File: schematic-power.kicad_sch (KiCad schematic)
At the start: 20 parts, among them U9 TPS62933

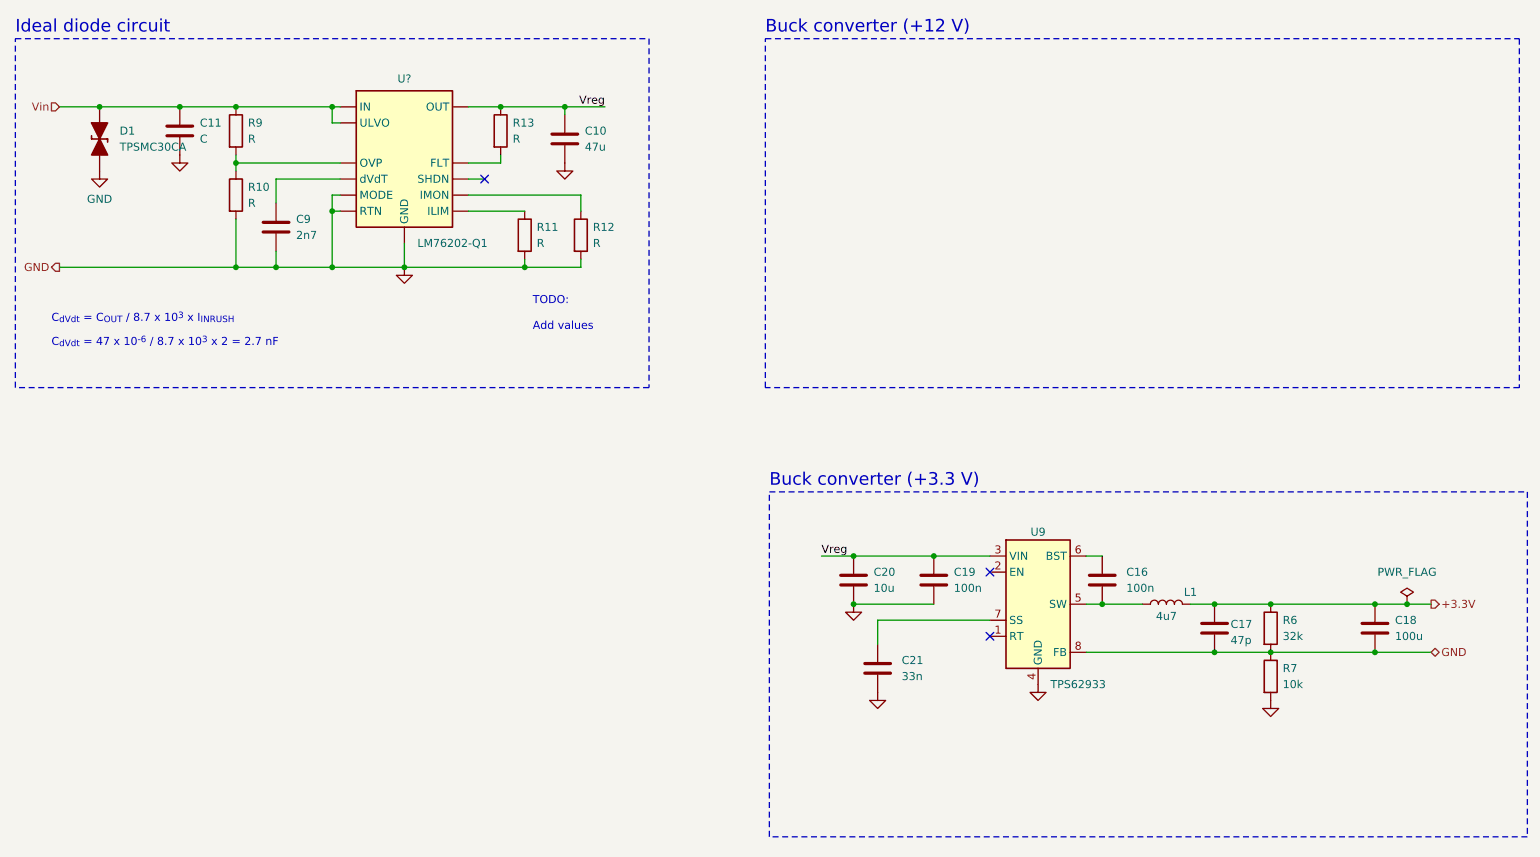
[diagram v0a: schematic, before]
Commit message: Add power stages
Valve, power supplay, fan
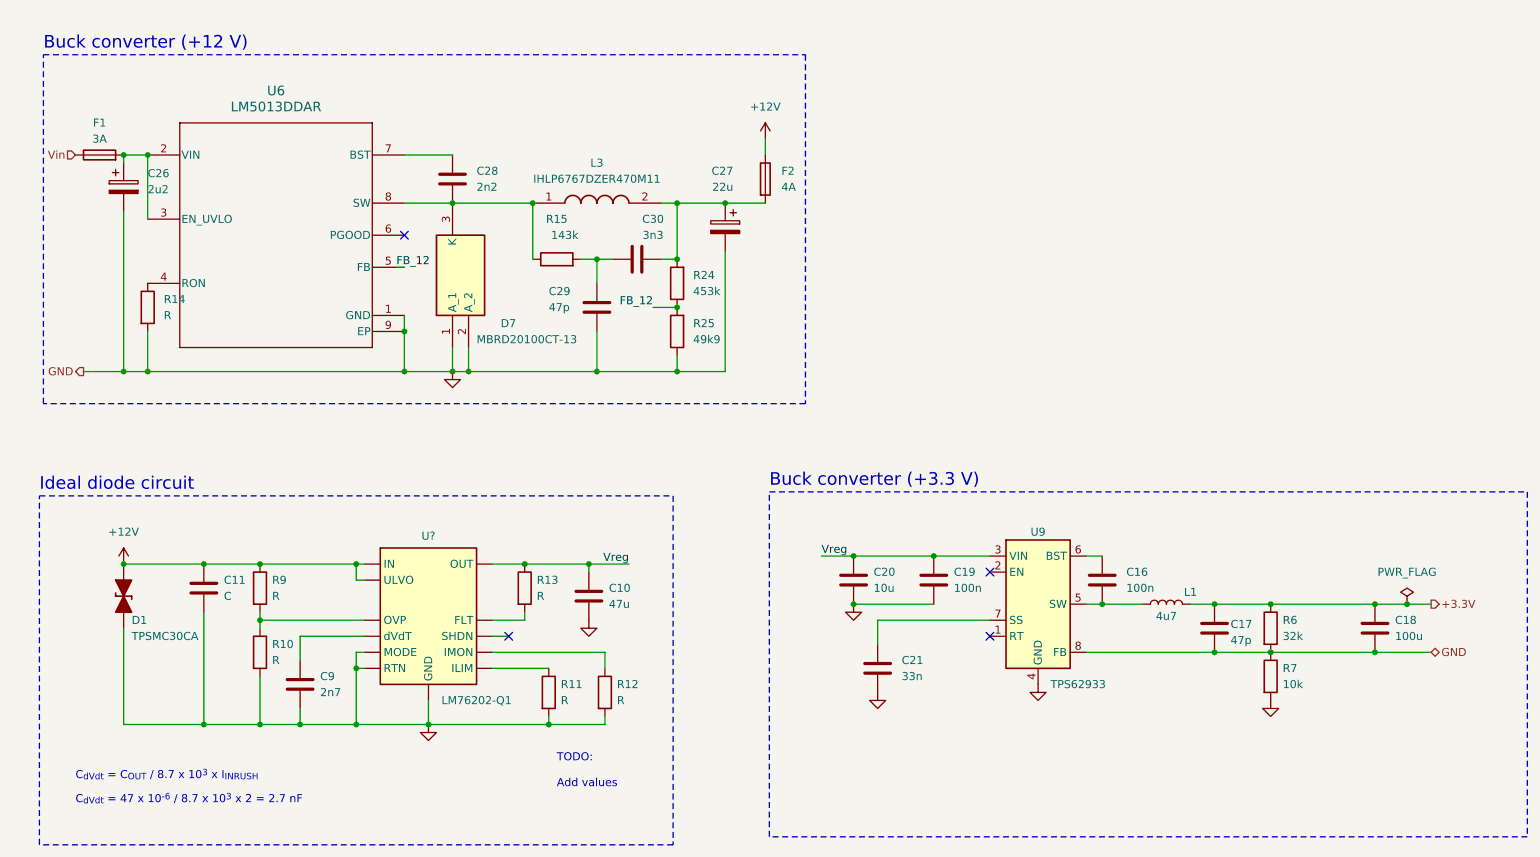
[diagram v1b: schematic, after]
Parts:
- added C26: 2u2, symbol Device:C_Polarized
- added C27: 22u, symbol Device:C_Polarized
- added C28: 2n2, symbol Device:C
- added C29: 47p, symbol Device:C
- added C30: 3n3, symbol Device:C
- added D7: MBRD20100CT-13, TO252_(DPAK)_1, symbol MBRD20100CT-13:MBRD20100CT-13
- added F1: 3A, symbol Device:Fuse
- added F2: 4A, symbol Device:Fuse
- added L3: IHLP6767DZER470M11, IHLP6767DZER470M11, symbol IHLP6767DZER470M11:IHLP6767DZER470M11
- added R14: R, symbol Device:R
- added R15: 143k, symbol Device:R
- added R24: 453k, symbol Device:R
- added R25: 49k9, symbol Device:R
- added U6: LM5013DDAR, DDA0008E-IPC_A, symbol 2023-11-20_17-31-45:LM5013DDAR
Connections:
- net GND: now also C26.2, C27.2, C29.1, D7.1 (A_1), D7.2 (A_2), R14.2, R25.1, U6.1 (GND), U6.9 (EP)
- net Vin: now also F1.1; no longer C11.1, D1.2 (A), R9.1, U?. (dVdT)
- new net: C28.1, D7.3 (K), L3.1, R15.1, U6.8 (SW)
- new net: C27.1, C30.2, F2.2, L3.2, R24.2
- new net: C26.1, F1.2, U6.2 (VIN), U6.3 (EN_UVLO)
- new net: C29.2, C30.1, R15.2
- new net: R14.1, U6.4 (RON)
- new net: C28.2, U6.7 (BST)
- new net +12V: C11.1, D1.2 (A), F2.1, R9.1, U?. (dVdT)
- new net FB_12: R24.1, R25.2, U6.5 (FB)
- no-connect marks 3 -> 4
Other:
- moved on the sheet: C10, C11, C9, D1, R10, R11, R12, R13, R9, U?

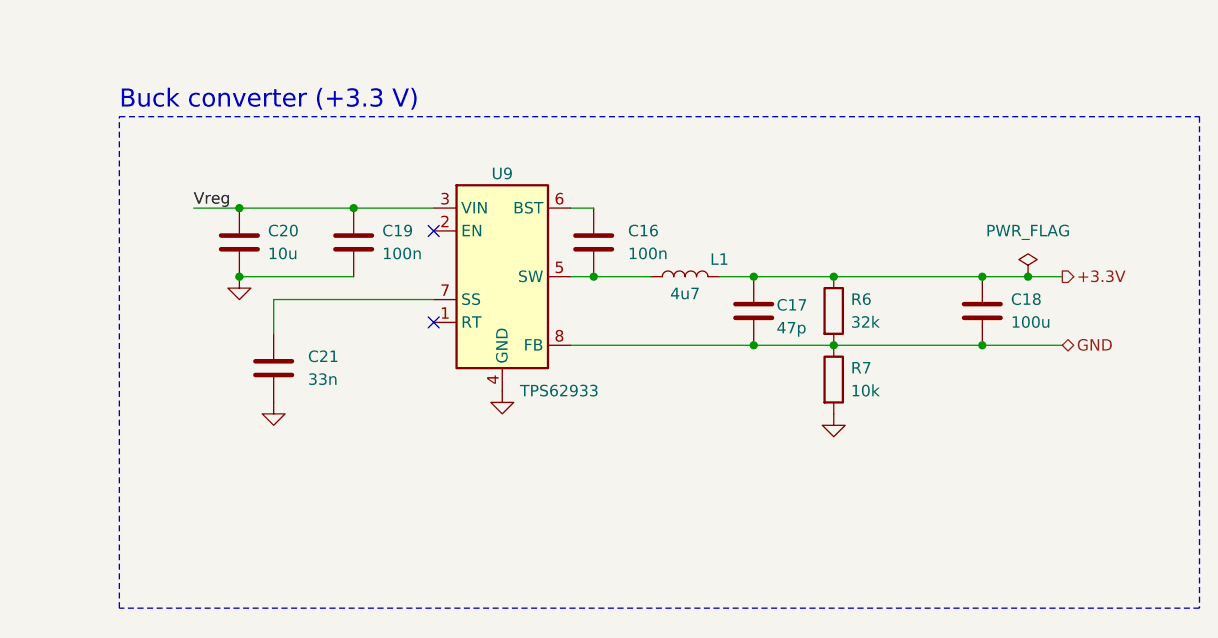
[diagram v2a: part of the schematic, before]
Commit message: Add Schottky Diode for VBUS and Vreg
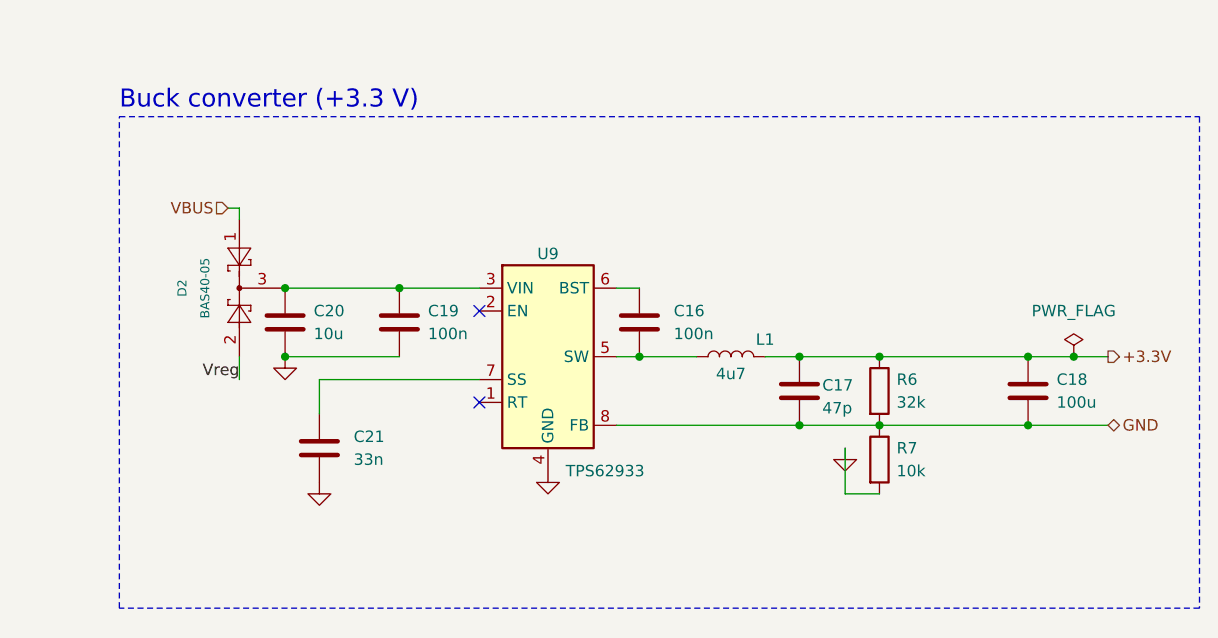
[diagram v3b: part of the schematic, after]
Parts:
- added D2: BAS40-05, Package_TO_SOT_SMD:SOT-23, symbol Diode:BAS40-04
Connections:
- net Vreg: now also D2.2; no longer C19.1, C20.1, U9.3 (VIN)
- new net: C19.1, C20.1, D2.3, U9.3 (VIN)
- new net VBUS: D2.1
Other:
- moved on the sheet: C16, C17, C18, C19, C20, C21, L1, R6, R7, U9

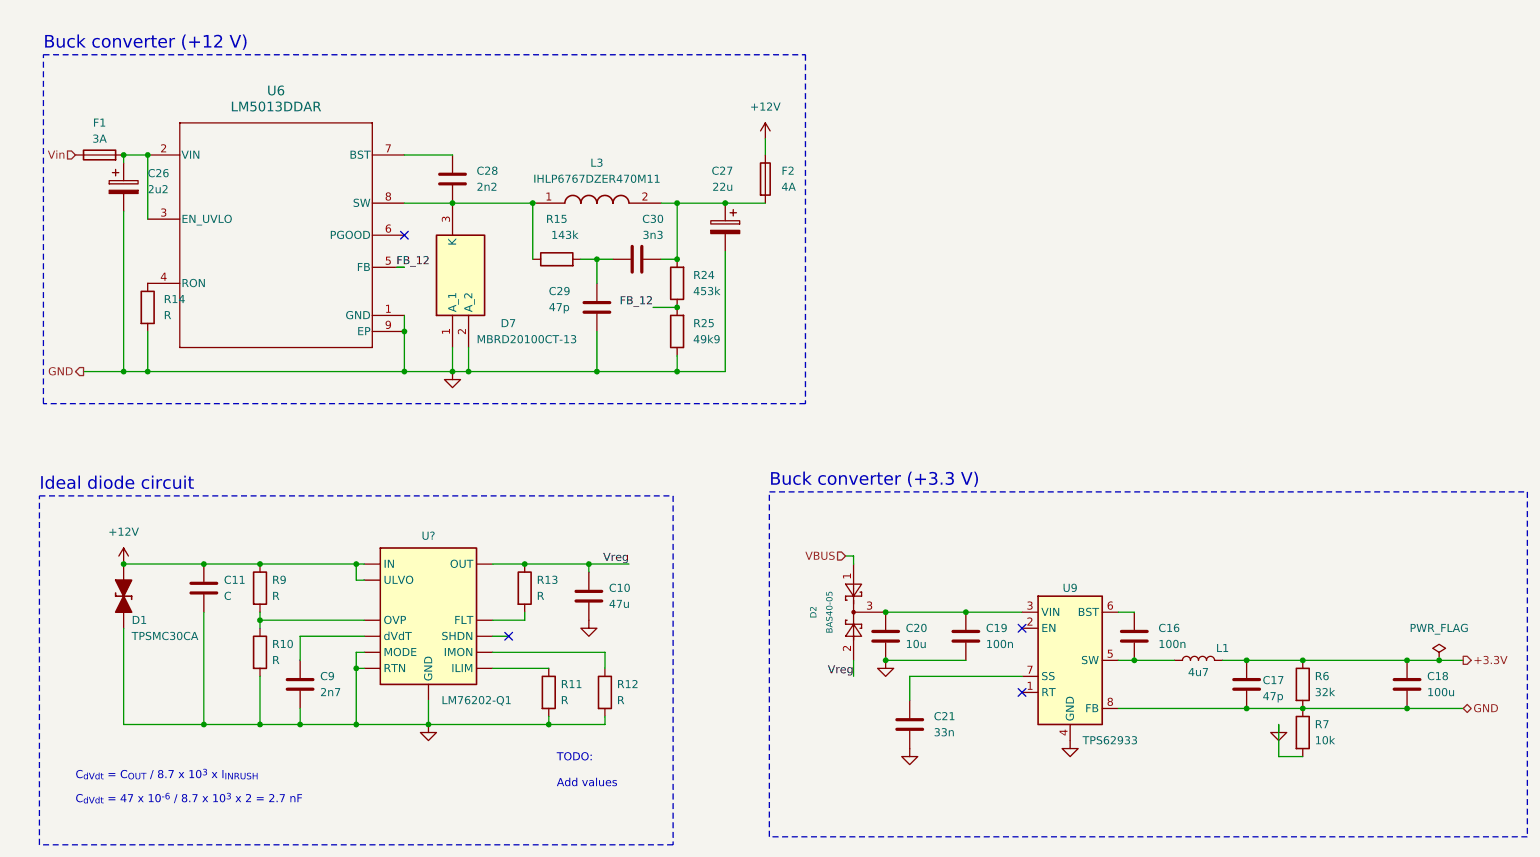
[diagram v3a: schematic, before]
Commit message: Add FC voltage measure, axilary input and output
Schematic complet?
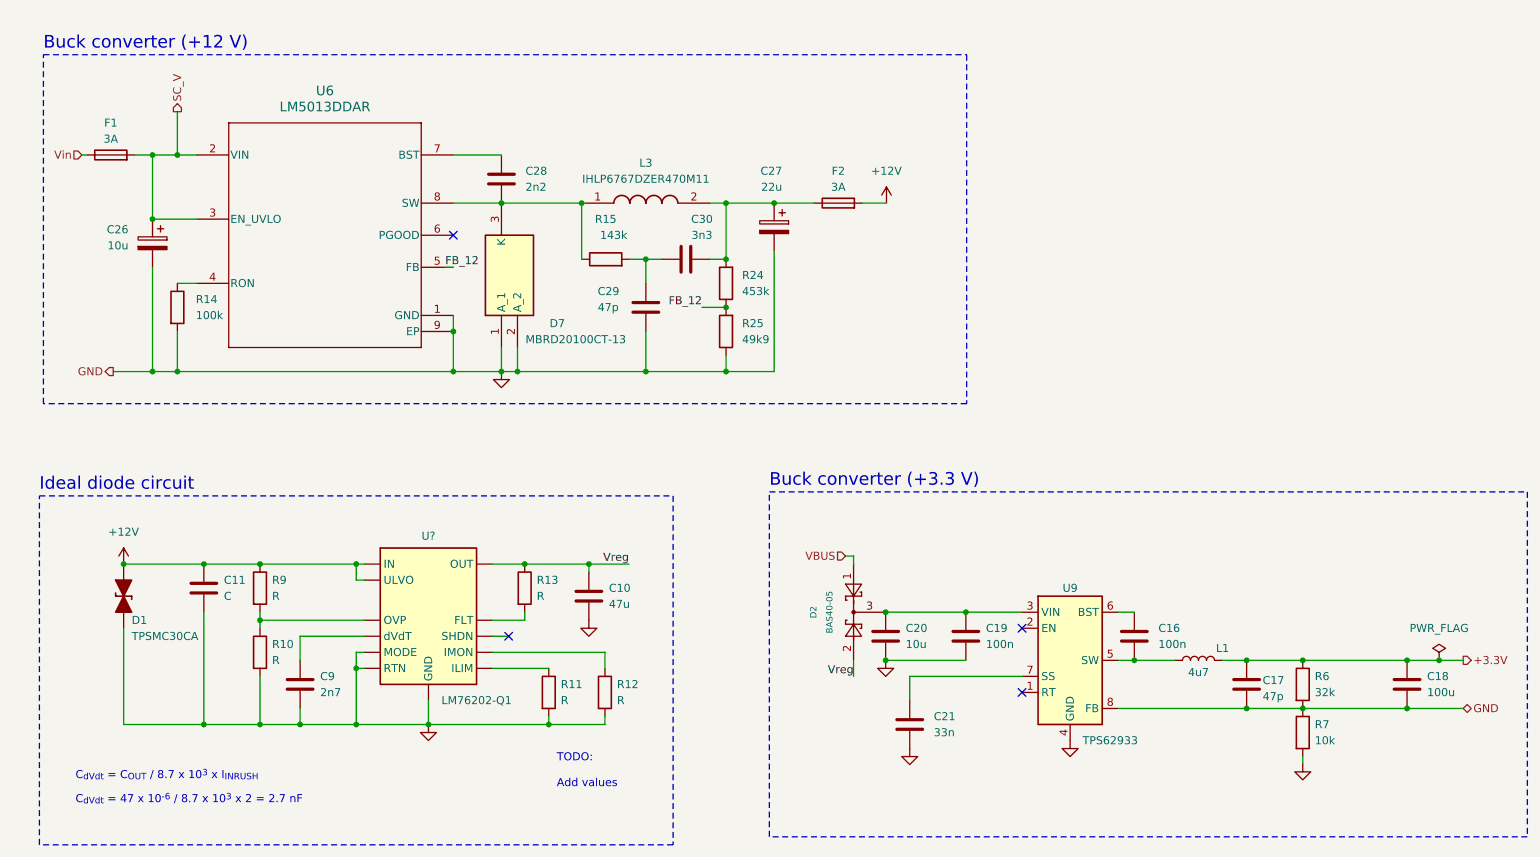
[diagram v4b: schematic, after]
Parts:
- C26: value 2u2 -> 10u
- F2: value 4A -> 3A
- R14: value R -> 100k
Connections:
- net +12V: now also F2.2; no longer F2.1
- net at C27.1, C30.2, L3.2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: now also F2.1; no longer F2.2
- net SC_V: now reaches C26.1, F1.2, U6.2 (VIN), U6.3 (EN_UVLO)
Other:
- title: Motor driver unit -> Fuel Cell Control Unit  (FCCU)
- moved on the sheet: C26, C27, C28, C29, C30, D7, F1, F2, L3, R14, R15, R24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

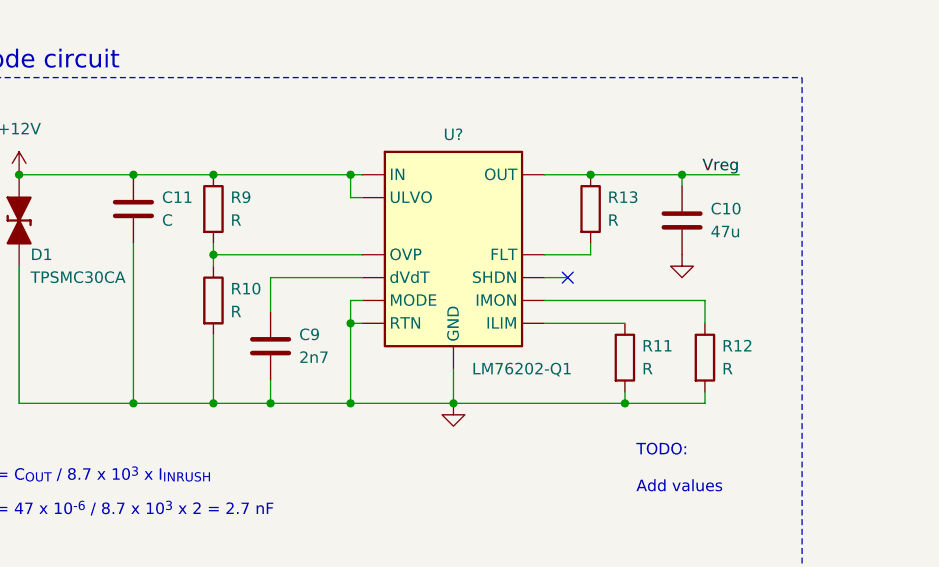
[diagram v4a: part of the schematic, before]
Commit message: First pcb, change fan conector
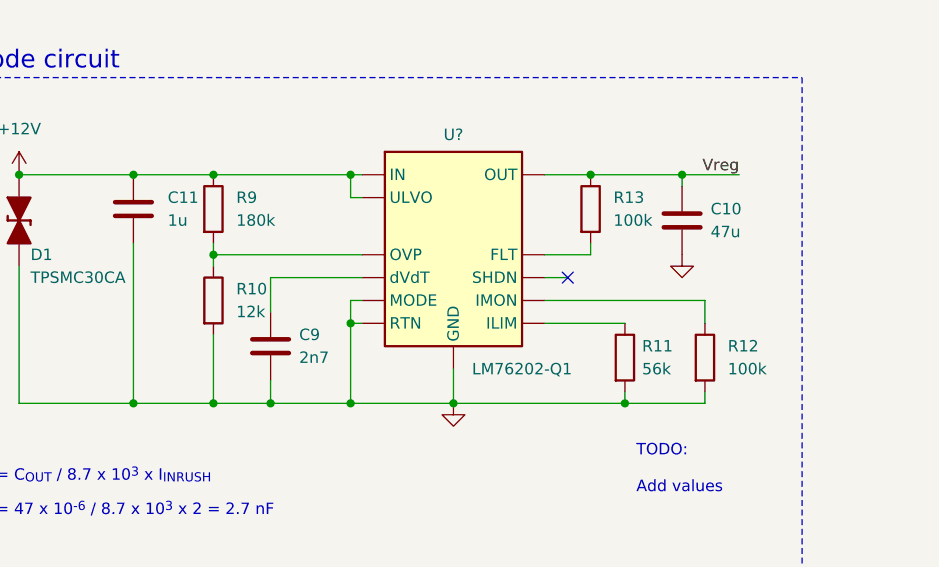
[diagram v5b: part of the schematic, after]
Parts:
- C10: footprint (none) -> Capacitor_SMD:CP_Elec_6.3x7.7
- C11: value C -> 1u; footprint (none) -> Capacitor_SMD:C_1206_3216Metric
- C16, C17, C19, C21, C28, C29, C30, C9: footprint (none) -> Capacitor_SMD:C_1206_3216Metric
- C18, C20, C26, C27: footprint (none) -> Capacitor_SMD:CP_Elec_8x10.5
- D7: footprint TO252_(DPAK)_1 -> (none)
- L1: footprint (none) -> Inductor_SMD:SRN3015TA4R7M
- L3: footprint IHLP6767DZER470M11 -> lib:IHLP6767DZER470M11
- R10: value R -> 12k; footprint (none) -> Resistor_SMD:R_1206_3216Metric
- R11: value R -> 56k; footprint (none) -> Resistor_SMD:R_1206_3216Metric
- R12, R13: value R -> 100k; footprint (none) -> Resistor_SMD:R_1206_3216Metric
- R14, R15, R6, R7: footprint (none) -> Resistor_SMD:R_1206_3216Metric
- R24, R25: footprint (none) -> LED_SMD:LED_1206_3216Metric
- R9: value R -> 180k; footprint (none) -> Resistor_SMD:R_1206_3216Metric
- U6: footprint DDA0008E-IPC_A -> Package_SO:Diodes_SO-8EP
- U?: footprint (none) -> Package_SO:VSSOP-8_3.0x3.0mm_P0.65mm
